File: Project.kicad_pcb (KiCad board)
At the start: 2 copper layers, 65 parts, among them J1 Screw_Terminal_01x02, J2 Screw_Terminal_01x02, J3 Conn_01x04_Socket, Q1 BT136-500, SW1 PEC11H, SW2 PEC11H, U1 AMS1117-3.3, U2 ESP32-WROOM-32, U3 MOC3021M, U4 MCT2E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

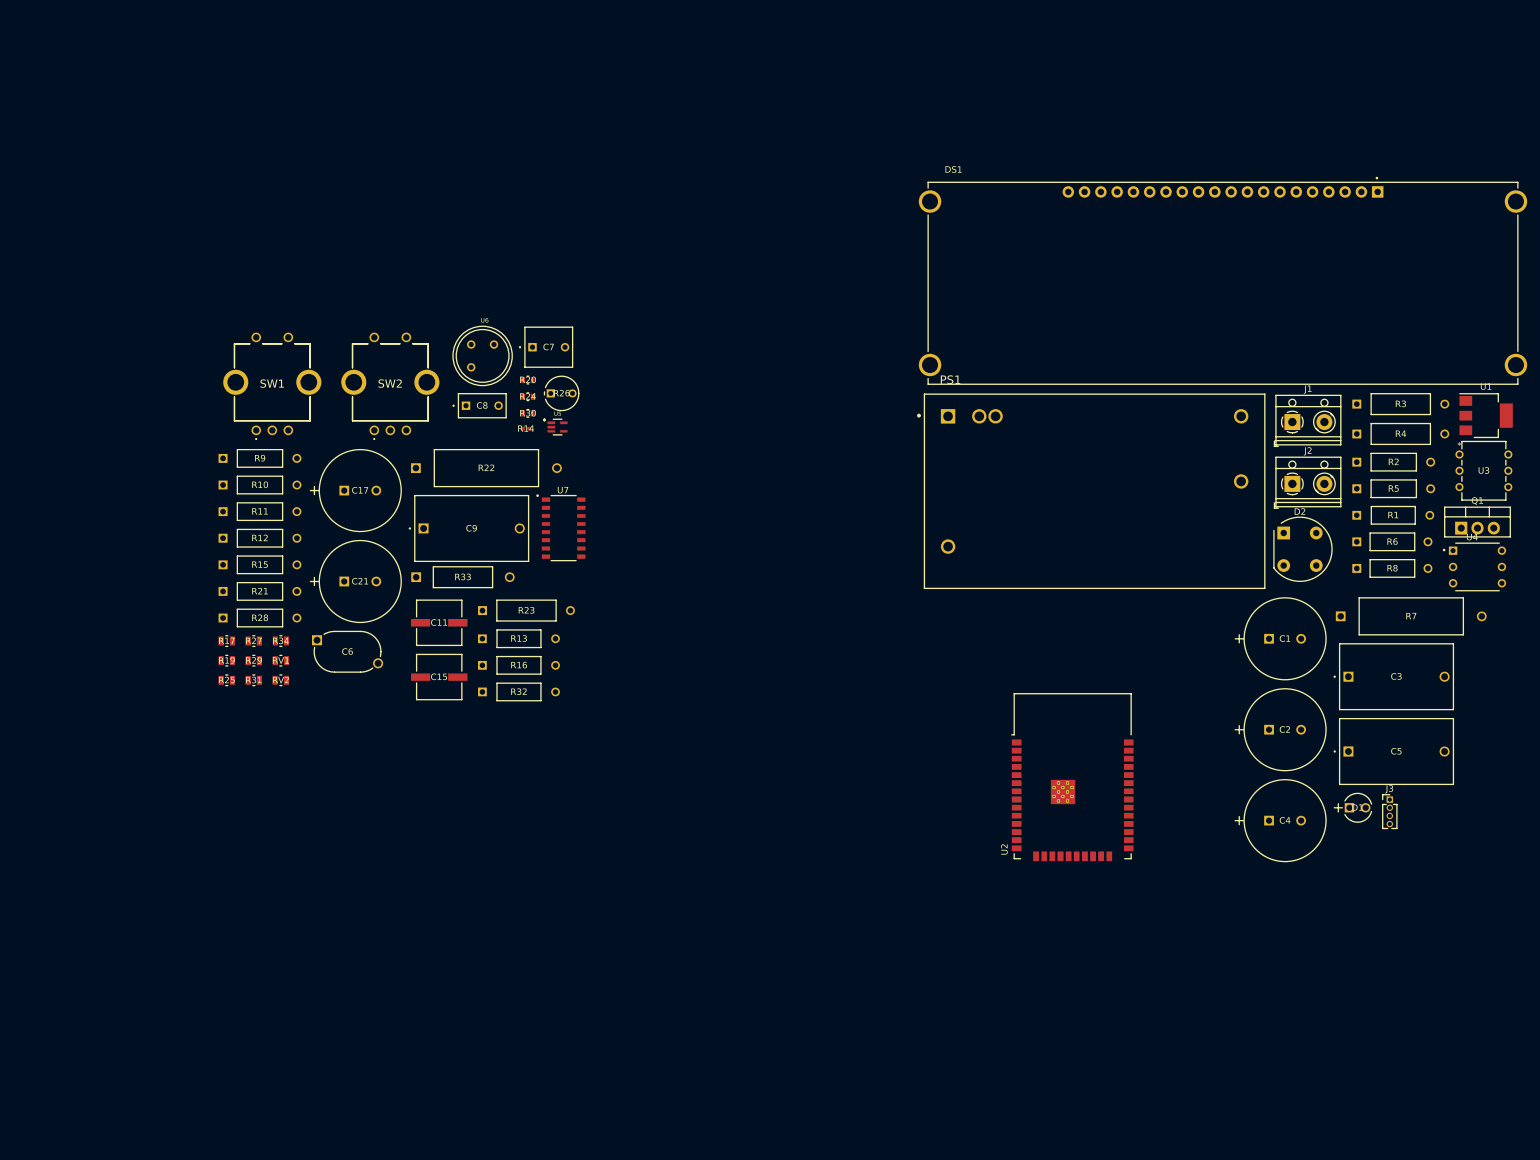
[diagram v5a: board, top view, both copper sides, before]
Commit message: PCB components arranged + Power traces
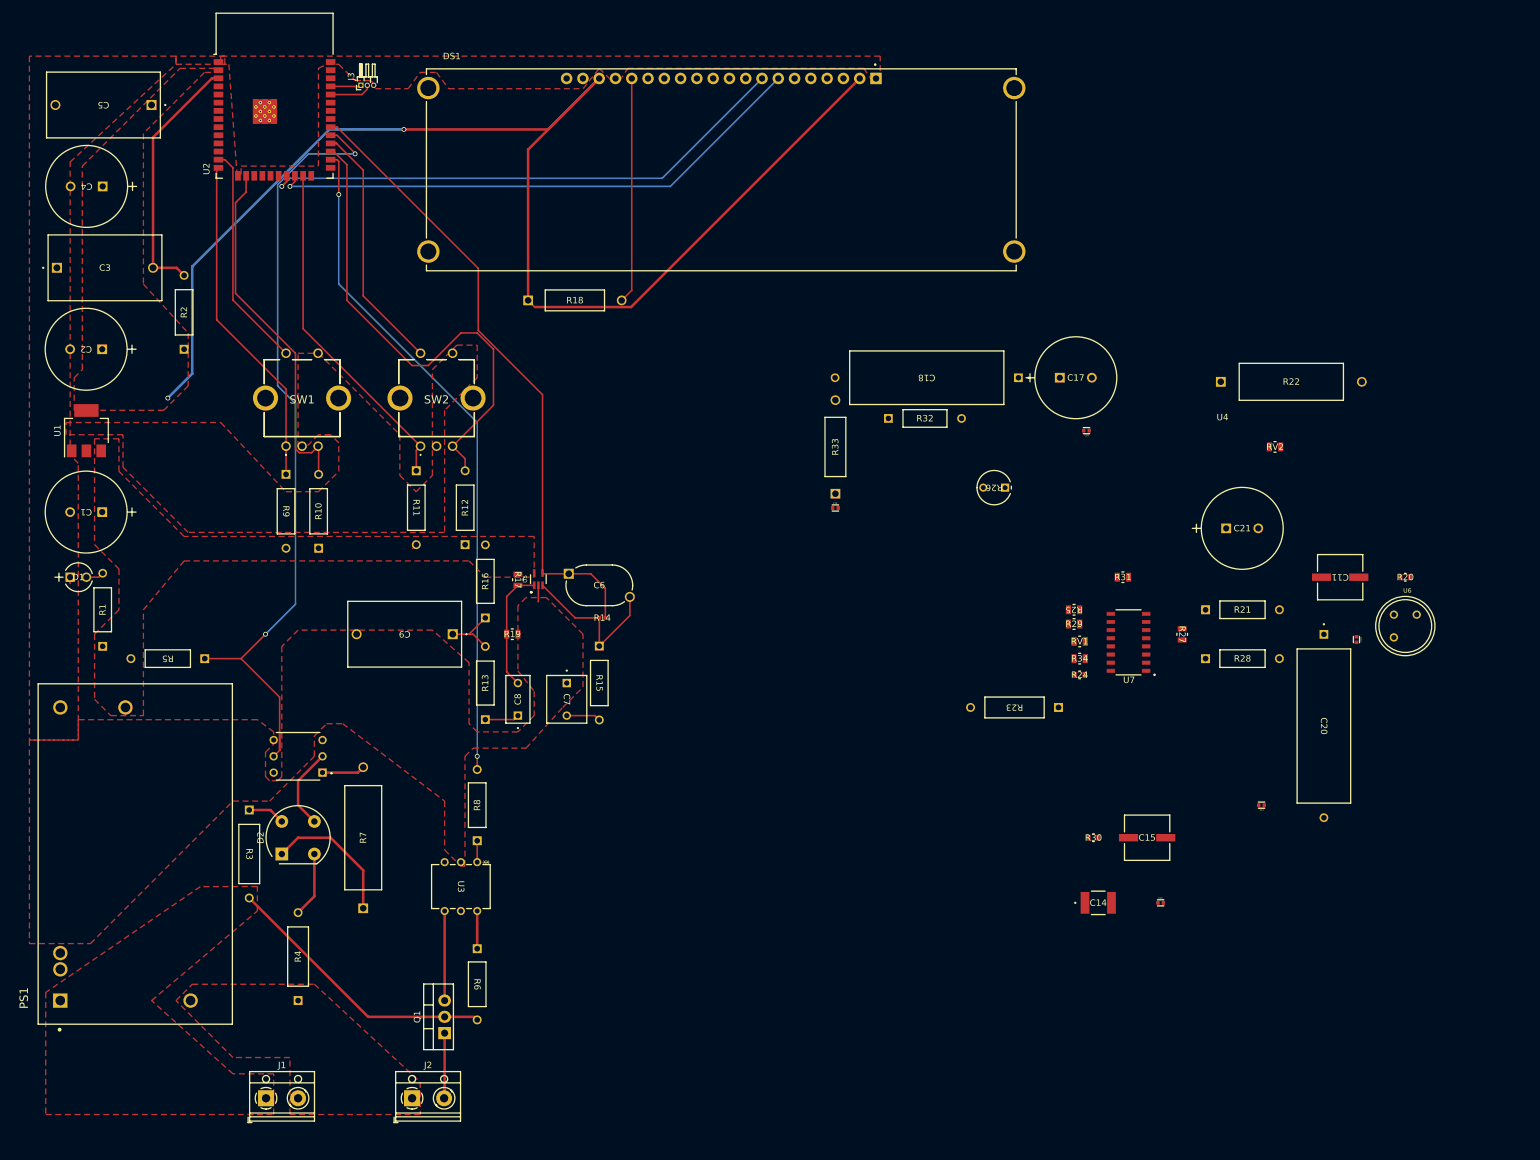
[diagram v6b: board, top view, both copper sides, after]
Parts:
- added C10: 103, Capacitor_10nF:CAPC1005X55N, F.Cu at (223.5, 111.3)
- added C12: 103, Capacitor_10nF:CAPC1005X55N, F.Cu at (208.7, 137.2)
- added C13: 103, Capacitor_10nF:CAPC1005X55N, F.Cu at (193.0, 152.4)
- added C14: 502, Capacitor_5nF:CAP_1812_AVX, F.Cu at (183.2, 152.4)
- added C16: 103, Capacitor_10nF:CAPC1005X55N, F.Cu at (181.4, 78.7)
- added C18: 104, Capacitor_100nF:WMF_08.1DX23.8LX0.6d_CND, F.Cu at (170.8, 70.5)
- added C19: 103, Capacitor_10nF:CAPC1005X55N, F.Cu at (142.2, 90.8)
- added C20: 104, Capacitor_100nF:WMF_08.1DX23.8LX0.6d_CND, F.Cu at (218.4, 110.5)
- added R18: 6.8k, Resistor_6_8k:RES_ROX1S_TYCO_TYC, F.Cu at (94.3, 58.4)
- J3: value Conn_01x04_Socket -> Conn_01x03_Pin; footprint Connector_PinHeader_1.27mm:PinHeader_1x04_P1.27mm_Vertical -> Connector_PinHeader_1.00mm:PinHeader_1x03_P1.00mm_Horizontal
- moved U1 218.4 mm to (25.4, 78.7), turned to 90 degrees
- moved C5 212.2 mm to (35.6, 27.9), turned to 180 degrees
- moved C3 211.3 mm to (20.8, 53.3)
- moved C4 207.1 mm to (27.9, 40.6), turned to 180 degrees
- moved D1 202.8 mm to (22.9, 101.6)
- moved R1 196.7 mm to (27.9, 112.4), turned to 90 degrees
- moved J3 195.4 mm to (68.2, 24.9), turned to 90 degrees
- moved J1 191.7 mm to (53.4, 182.9)
- moved C2 191.5 mm to (27.9, 66.0), turned to 180 degrees
- moved R4 187.3 mm to (58.4, 167.6), turned to 90 degrees
- moved U4 186.3 mm to (58.4, 129.5), turned to 180 degrees
- moved R3 184.0 mm to (50.8, 137.9), turned to -90 degrees
- moved R2 183.8 mm to (40.6, 66.0), turned to 90 degrees
- moved C1 183.1 mm to (27.9, 91.4), turned to 180 degrees
- moved R5 181.7 mm to (43.9, 114.3), turned to 180 degrees
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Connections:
- C1 pad 1: VCC_5V -> VDD5
- C2 pad 1: VCC33 -> VDD33
- DS1 pad 1: Net-(DS1-VSS-Pad1) -> GND
- DS1 pad 16: unconnected-(DS1-~{RES}-Pad16) -> Net-(DS1-~{RES})
- DS1 pad 17: unconnected-(DS1-BS0-Pad17) -> GND
- DS1 pad 18: unconnected-(DS1-BS1-Pad18) -> VDD33
- DS1 pad 19: unconnected-(DS1-BS2-Pad19) -> GND
- DS1 pad 2: unconnected-(DS1-VDD-Pad2) -> VDD33
- DS1 pad 20: Net-(DS1-VSS-Pad1) -> GND
- DS1 pad 7: unconnected-(DS1-DB0/SCLK/SCL-Pad7) -> I2CCP
- DS1 pad 8: unconnected-(DS1-DB1/SDI/SDAIN-Pad8) -> I2CDP
- J3 pad 1: VDD5 -> UART_TX
- J3 pad 2: ZC -> UART_RX
- R1 pad 1: VCC_5V -> VDD5
- U1 pad 2: VCC33 -> VDD33
- U1 pad 3: VCC_5V -> VDD5
- U2 pad 21: unconnected-(U2-SDO/SD0-Pad21) -> I2CDP
- U2 pad 22: unconnected-(U2-SDI/SD1-Pad22) -> I2CCP
- U2 pad 34: unconnected-(U2-RXD0/IO3-Pad34) -> UART_RX
- U2 pad 35: unconnected-(U2-TXD0/IO1-Pad35) -> UART_TX
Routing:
- net VDD33: track 0.00 -> 204.6 mm, vias 0 -> 2
- net ZC: track 0.00 -> 124.2 mm, vias 0 -> 2
- net TRIAC_1: track 0.00 -> 105.2 mm, vias 0 -> 2
- net MIC: track 0.00 -> 99.2 mm
- net I2CCP: track 0.00 -> 85.1 mm, vias 0 -> 1
- net I2CDP: track 0.00 -> 83.9 mm, vias 0 -> 1
- net ENC2_1: track 0.00 -> 77.2 mm
- net ENC1_1: track 0.00 -> 55.8 mm
- net ENC2_2: track 0.00 -> 53.9 mm
- net ENC1_2: track 0.00 -> 52.0 mm
- net AC230P: track 0.00 -> 43.4 mm
- net SW2: track 0.00 -> 40.1 mm
- net Net-(U2-EN): track 0.00 -> 39.7 mm
- net Net-(DS1-~{RES}): track 0.00 -> 35.3 mm
- net SW1: track 0.00 -> 35.1 mm
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- added copper zone on F.Cu, net AC230N
- added copper zone on F.Cu, net AC230P
- added copper zone on F.Cu, net GND
- added copper zone on F.Cu, net VDD33
- added copper zone on F.Cu, net VDD5

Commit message: PCB finished
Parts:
- added JP1: Jumper_3_Open, Jumper:SolderJumper-3_P1.3mm_Open_Pad1.0x1.5mm, F.Cu at (147.3, 102.8)
- RV1, RV2: footprint Resistor_1M:RES0805_CRG_TYCO_TYC -> Potentiometer_SMD:Potentiometer_Bourns_3214W_Vertical
- moved R20 87.3 mm to (153.6, 61.5), turned to 90 degrees
- moved R22 86.8 mm to (121.9, 103.6), turned to 90 degrees
- moved U6 85.7 mm to (160.0, 61.5), turned to 90 degrees
- moved C10 77.0 mm to (160.0, 67.9), turned to 0 degrees
- moved C12 75.7 mm to (144.7, 96.7), turned to -90 degrees
- moved C11 75.5 mm to (148.0, 82.5), turned to -90 degrees
- moved C17 71.8 mm to (121.2, 115.4), turned to 90 degrees
- moved C18 71.4 mm to (121.2, 121.9), turned to -90 degrees
- moved R21 70.2 mm to (136.4, 76.8)
- moved C21 69.4 mm to (134.0, 88.9)
- moved R32 69.2 mm to (127.6, 142.2), turned to 90 degrees
- moved C20 65.2 mm to (154.3, 99.0)
- moved RV2 65.1 mm to (146.6, 92.0), turned to 90 degrees
- moved R33 61.9 mm to (139.3, 150.4), turned to 180 degrees
- moved C16 61.3 mm to (129.5, 111.3), turned to -90 degrees
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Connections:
- SW1 pad A1: (no net) -> ENC1_2
- SW1 pad B1: (no net) -> ENC1_1
- SW2 pad A1: (no net) -> ENC2_2
- SW2 pad B1: (no net) -> ENC2_1
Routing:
- net PIR_SENS: track 0.00 -> 79.7 mm
- net Net-(U6-S): track 0.00 -> 73.5 mm, vias 0 -> 2
- net Net-(U7-2IN-): track 0.00 -> 53.3 mm
- net Net-(U7-2OUT): track 0.00 -> 45.4 mm
- net Net-(U7-1IN-): track 0.00 -> 41.3 mm
- net Net-(U7-1OUT): track 0.00 -> 26.0 mm
- net Net-(R28-Pad2): track 0.00 -> 22.8 mm
- net Net-(U7-VO): track 0.00 -> 21.4 mm
- net Net-(U7-RC2): track 0.00 -> 21.3 mm, vias 0 -> 2
- net Net-(U7-RR1): track 0.00 -> 20.9 mm
- net VDD5: track 1.53 -> 21.7 mm, vias 0 -> 6
- net VDD33: track 204.6 -> 224.4 mm, vias 2 -> 3
- net Net-(C11-Pad1): track 0.00 -> 19.7 mm
- net ENC2_1: track 77.2 -> 58.8 mm
- net Net-(C17-Pad1): track 0.00 -> 18.0 mm
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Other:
- board outline added: 158.8 x 172.1 mm

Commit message: Generated Gerber files
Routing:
- net GND: track 15.4 -> 19.5 mm, vias 0 -> 1
- added copper zone on B.Cu, net GND
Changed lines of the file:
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@@
       (usegerberattributes true)
       (usegerberadvancedattributes true)
-      (creategerberjobfile true)
+      (creategerberjobfile false)
       (dashed_line_dash_ratio 12.000000)
       (dashed_line_gap_ratio 3.000000)
@@
       (outputformat 1)
       (mirror false)
-      (drillshape 1)
+      (drillshape 0)
       (scaleselection 1)
-      (outputdirectory "")
+      (outputdirectory "Gerber Files/")
     )
   )
@@
     (fp_arc (start 3.925916 2.548276) (mid 3.029459 3.01425) (end 2.032 3.175)
       (stroke (width 0.1524) (type solid)) (layer "F.SilkS"))
-    (fp_arc (start 5.207 0) (mid 5.18497 0.373374) (end 5.119184 0.741566)
+    (fp_arc (start 5.207 0) (mid 5.184969 0.373374) (end 5.119184 0.741566)
       (stroke (width 0.1524) (type solid)) (layer "F.SilkS"))
     (fp_line (start -5.8039 -3.302) (end 5.8039 -3.302)
@@
   (segment (start 169.938811 99.69889) (end 167.33231 97.092389) (width 0.25) (layer "F.Cu") (net 1))
   (segment (start 22.86 101.6) (end 22.86 102.61) (width 0.25) (layer "F.Cu") (net 1))
+  (segment (start 21.33 121.92) (end 25.4 121.92) (width 0.25) (layer "F.Cu") (net 1))
   (segment (start 169.938811 102.235) (end 169.938811 106.286189) (width 0.25) (layer "F.Cu") (net 1))
   (segment (start 167.33231 97.092389) (end 167.577389 97.092389) (width 0.25) (layer "F.Cu") (net 1))
@@
   (segment (start 137.555611 125.2871) (end 137.758811 125.4903) (width 0.25) (layer "F.Cu") (net 1))
   (segment (start 169.938811 106.286189) (end 169.545 106.68) (width 0.25) (layer "F.Cu") (net 1))
+  (via (at 25.4 121.92) (size 0.75) (drill 0.5) (layers "F.Cu" "B.Cu") (net 1))
   (segment (start 45 23.77) (end 46 23.77) (width 0.4) (layer "F.Cu") (net 4))
   (segment (start 35.795601 32.974399) (end 45 23.77) (width 0.4) (layer "F.Cu") (net 4))
@@
   (segment (start 27.3177 101.6) (end 27.94 100.9777) (width 0.25) (layer "F.Cu") (net 6))
   (segment (start 25.4 101.6) (end 27.3177 101.6) (width 0.25) (layer "F.Cu") (net 6))
-  (segment (start 63.5 142.24) (end 68.58 147.32) (width 0.4) (layer "F.Cu") (net 7))
-  (segment (start 55.88 144.78) (end 58.42 142.24) (width 0.4) (layer "F.Cu") (net 7))
-  (segment (start 58.42 142.24) (end 63.5 142.24) (width 0.4) (layer "F.Cu") (net 7))
-  (segment (start 68.58 147.32) (end 68.58 153.24074) (width 0.4) (layer "F.Cu") (net 7))
-  (segment (start 58.42 153.91892) (end 60.96 151.37892) (width 0.4) (layer "F.Cu") (net 8))
-  (segment (start 60.96 151.37892) (end 60.96 144.78) (width 0.4) (layer "F.Cu") (net 8))
-  (segment (start 58.42 133.35) (end 62.23 129.54) (width 0.4) (layer "F.Cu") (net 9))
-  (segment (start 58.42 137.16) (end 58.42 133.35) (width 0.4) (layer "F.Cu") (net 9))
-  (segment (start 60.96 139.7) (end 58.42 137.16) (width 0.4) (layer "F.Cu") (net 9))
-  (segment (start 50.8 137.91946) (end 54.09946 137.91946) (width 0.4) (layer "F.Cu") (net 10))
-  (segment (start 54.09946 137.91946) (end 55.88 139.7) (width 0.4) (layer "F.Cu") (net 10))
-  (segment (start 69.33946 170.18) (end 50.8 151.64054) (width 0.4) (layer "F.Cu") (net 11))
-  (segment (start 81.28 170.18) (end 85.88883 170.18) (width 0.4) (layer "F.Cu") (net 11))
-  (segment (start 81.28 170.18) (end 69.33946 170.18) (width 0.4) (layer "F.Cu") (net 11))
+  (segment (start 63.5 142.24) (end 68.58 147.32) (width 0.8) (layer "F.Cu") (net 7))
+  (segment (start 55.88 144.78) (end 58.42 142.24) (width 0.8) (layer "F.Cu") (net 7))
+  (segment (start 58.42 142.24) (end 63.5 142.24) (width 0.8) (layer "F.Cu") (net 7))
+  (segment (start 68.58 147.32) (end 68.58 153.24074) (width 0.8) (layer "F.Cu") (net 7))
+  (segment (start 58.42 153.91892) (end 60.96 151.37892) (width 0.8) (layer "F.Cu") (net 8))
+  (segment (start 60.96 151.37892) (end 60.96 144.78) (width 0.8) (layer "F.Cu") (net 8))
+  (segment (start 58.42 133.35) (end 62.23 129.54) (width 0.8) (layer "F.Cu") (net 9))
+  (segment (start 58.42 137.16) (end 58.42 133.35) (width 0.8) (layer "F.Cu") (net 9))
+  (segment (start 60.96 139.7) (end 58.42 137.16) (width 0.8) (layer "F.Cu") (net 9))
+  (segment (start 50.8 137.91946) (end 54.09946 137.91946) (width 0.8) (layer "F.Cu") (net 10))
+  (segment (start 54.09946 137.91946) (end 55.88 139.7) (width 0.8) (layer "F.Cu") (net 10))
+  (segment (start 69.33946 170.18) (end 50.8 151.64054) (width 0.8) (layer "F.Cu") (net 11))
+  (segment (start 81.28 170.18) (end 85.88883 170.18) (width 0.8) (layer "F.Cu") (net 11))
+  (segment (start 81.28 170.18) (end 69.33946 170.18) (width 0.8) (layer "F.Cu") (net 11))
   (segment (start 85.88883 170.18) (end 86.36 170.65117) (width 0.2) (layer "F.Cu") (net 11))
-  (segment (start 81.28 172.72) (end 81.28 182.8) (width 0.4) (layer "F.Cu") (net 13))
+  (segment (start 81.28 172.72) (end 81.28 182.8) (width 0.8) (layer "F.Cu") (net 13))
   (segment (start 81.28 182.8) (end 81.2 182.88) (width 0.25) (layer "F.Cu") (net 13))
   (segment (start 92.2052 101.1206) (end 92.71 101.1206) (width 0.25) (layer "F.Cu") (net 14))
@@
   (segment (start 86.36 129.54) (end 86.36 77.456801) (width 0.25) (layer "B.Cu") (net 16))
   (segment (start 64.77 55.866801) (end 64.77 41.91) (width 0.25) (layer "B.Cu") (net 16))
-  (segment (start 81.28 167.64) (end 81.28 153.67) (width 0.4) (layer "F.Cu") (net 17))
-  (segment (start 86.36 159.54883) (end 86.36 153.67) (width 0.4) (layer "F.Cu") (net 18))
+  (segment (start 81.28 167.64) (end 81.28 153.67) (width 0.8) (layer "F.Cu") (net 17))
+  (segment (start 86.36 159.54883) (end 86.36 153.67) (width 0.8) (layer "F.Cu") (net 18))
   (segment (start 67.73926 132.08) (end 68.58 131.23926) (width 0.4) (layer "F.Cu") (net 19))
-  (segment (start 62.23 132.08) (end 67.73926 132.08) (width 0.4) (layer "F.Cu") (net 19))
-  (segment (start 86.36 146.05) (end 86.36 142.71117) (width 0.25) (layer "F.Cu") (net 20))
+  (segment (start 62.23 132.08) (end 67.73926 132.08) (width 0.8) (layer "F.Cu") (net 19))
+  (segment (start 86.36 146.05) (end 86.36 142.71117) (width 0.8) (layer "F.Cu") (net 20))
   (segment (start 48.26 37.73) (end 47 36.47) (width 0.25) (layer "F.Cu") (net 30))
   (segment (start 48.26 58.379569) (end 48.26 37.73) (width 0.25) (layer "F.Cu") (net 30))
@@
         (xy 147.955 104.14)
         (xy 135.89 104.14)
-        (xy 135.89 104.14)
         (xy 124.46 104.14)
         (xy 123.19 105.41)
@@
       )
     )
+  )
+  (zone (net 1) (net_name "GND") (layer "B.Cu") (hatch edge 0.5)
+    (priority 15)
+    (connect_pads (clearance 0.5))
+    (min_thickness 0.25) (filled_areas_thickness no)
+    (fill yes (thermal_gap 0.5) (thermal_bridge_width 0.5))
+    (polygon
+      (pts
+        (xy 13.97 18.542)
+        (xy 13.97 190.5)
+        (xy 171.45 190.5)
+        (xy 172.727679 190.507679)
+        (xy 172.72 19.05)
+        (xy 172.72 18.542)
+      )
+    )
